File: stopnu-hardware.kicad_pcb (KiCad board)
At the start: 4 copper layers, 94 x 131 mm, 108 parts, among them CN1 SM04B-SRSS-TB (LF)(SN), CN2 OQ0232510000G, CN3 OQ0232510000G, CN4 OQ0232510000G, CN5 OQ0232510000G, CN6 OQ0232510000G, CN7 OQ0232510000G, CN8 OQ0232510000G, J1 Conn_02x15_Odd_Even, J2 Conn_01x02_Pin, U1 WIFI_KIT_32__V3_, U19 SY6280AAC, U2 74HCT1G125GW-Q100H, U3 LD1117V33, U4 74HCT1G125GW-Q100H, U5 LTV-817S, U6 LTV-817S, U7 LTV-817S, U8 MPU-6050_C24112

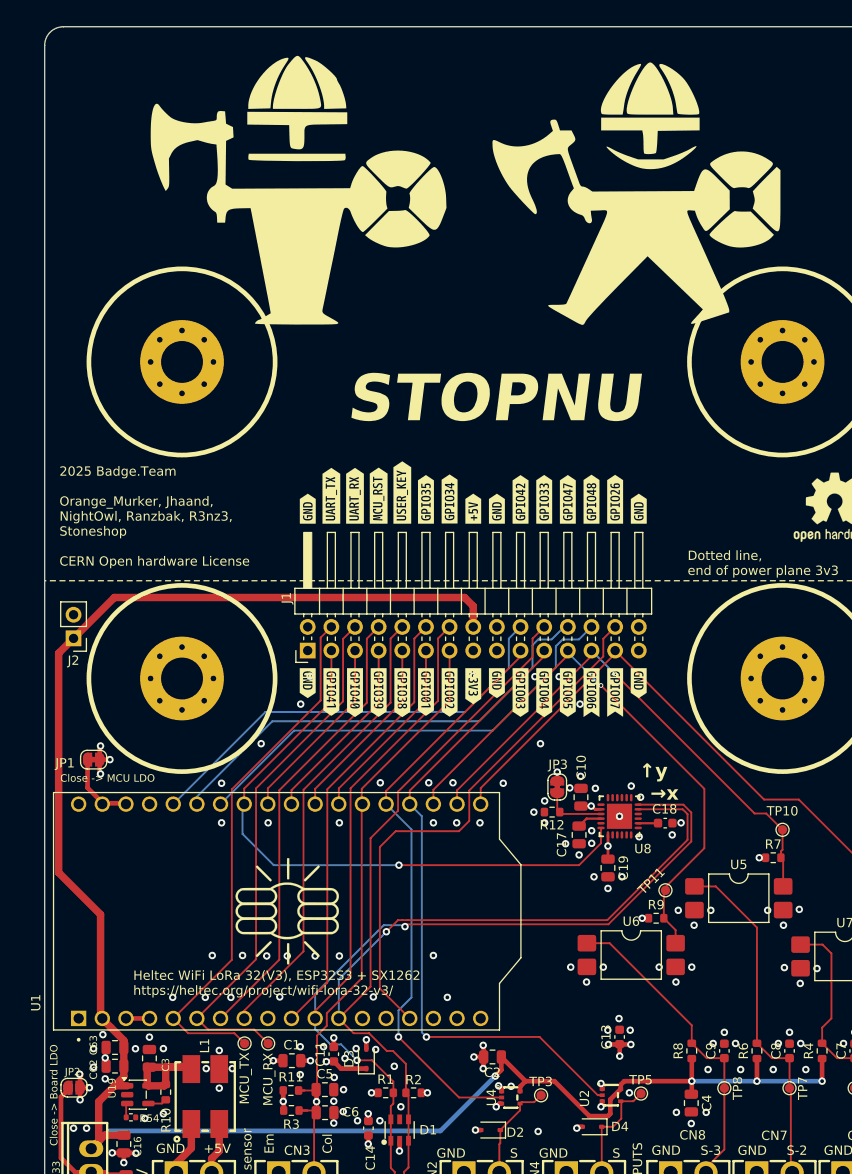
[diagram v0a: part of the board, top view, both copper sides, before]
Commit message: Update viking footprint art.
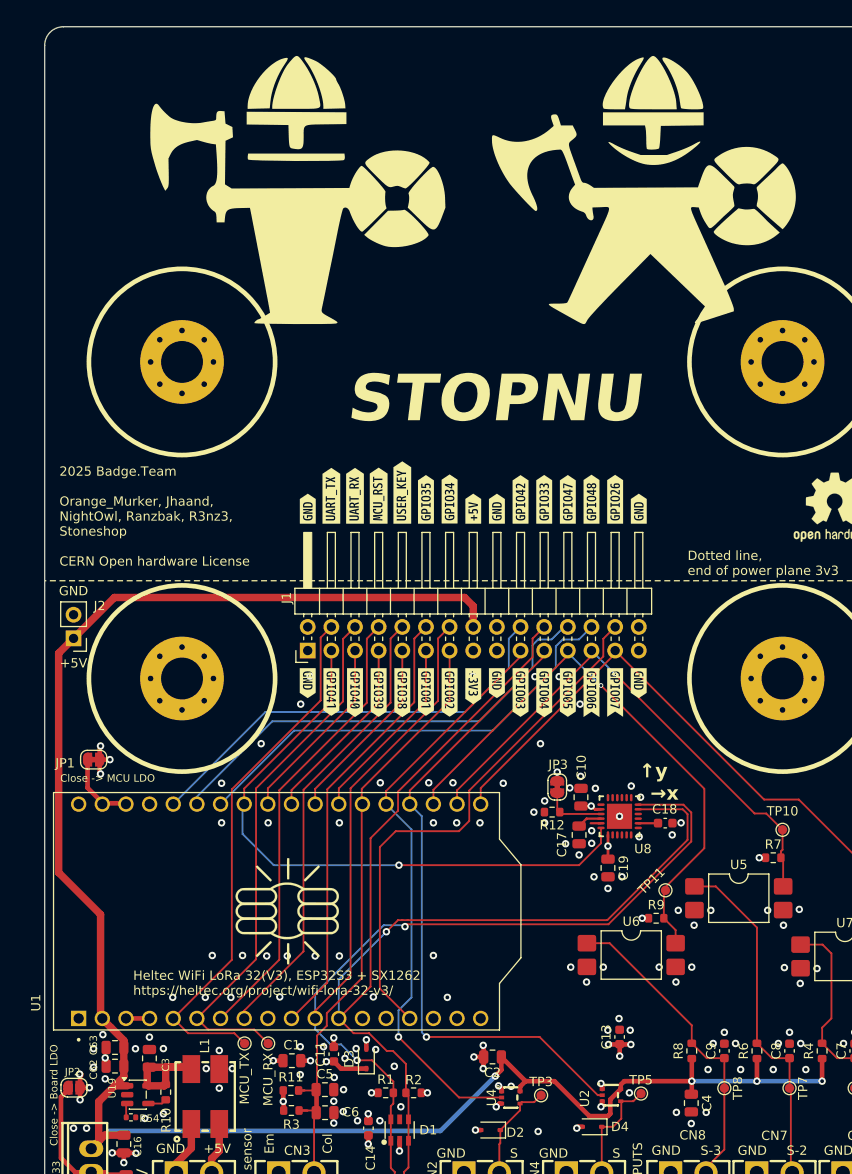
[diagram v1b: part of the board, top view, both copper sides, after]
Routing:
- net /GPIO02: track 67.8 -> 66.6 mm, vias 1 -> 0
- net GND: track 24.3 -> 25.4 mm
- net Net-(JP3-B): track 6.67 -> 6.00 mm

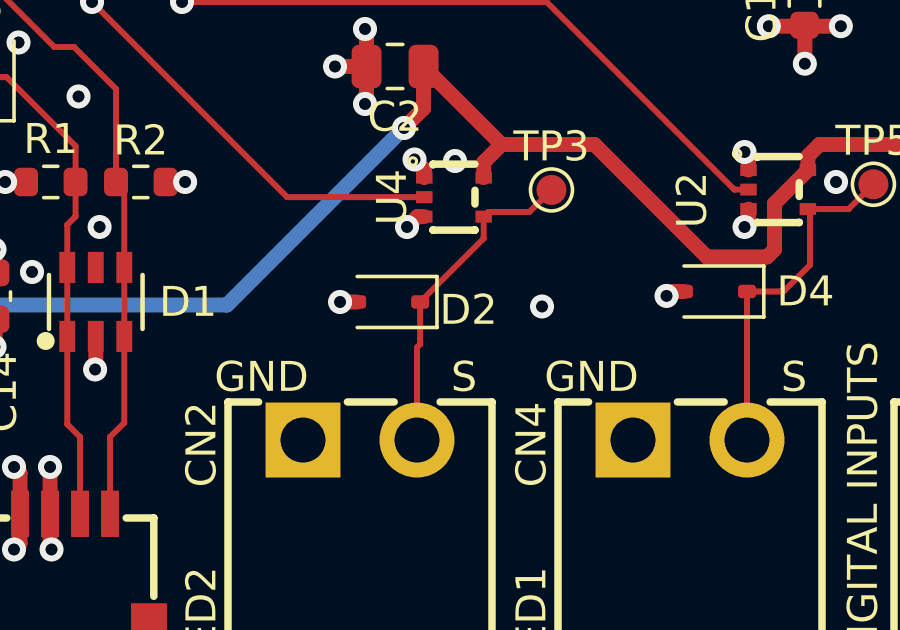
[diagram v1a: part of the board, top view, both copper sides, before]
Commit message: Straightened a track between D2 and CN2
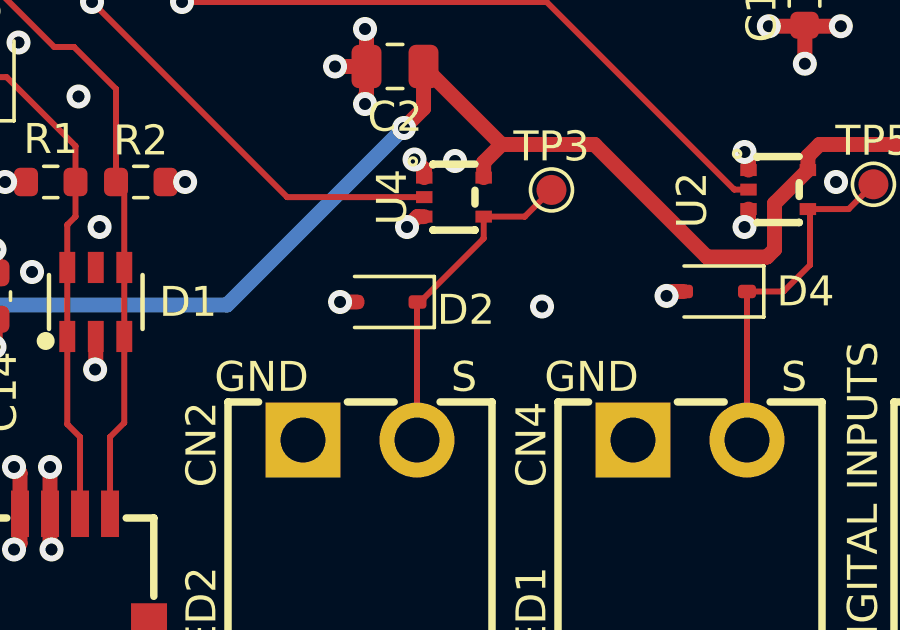
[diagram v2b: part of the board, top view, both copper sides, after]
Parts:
- moved D2 0.09 mm to (0.80, 65.5)

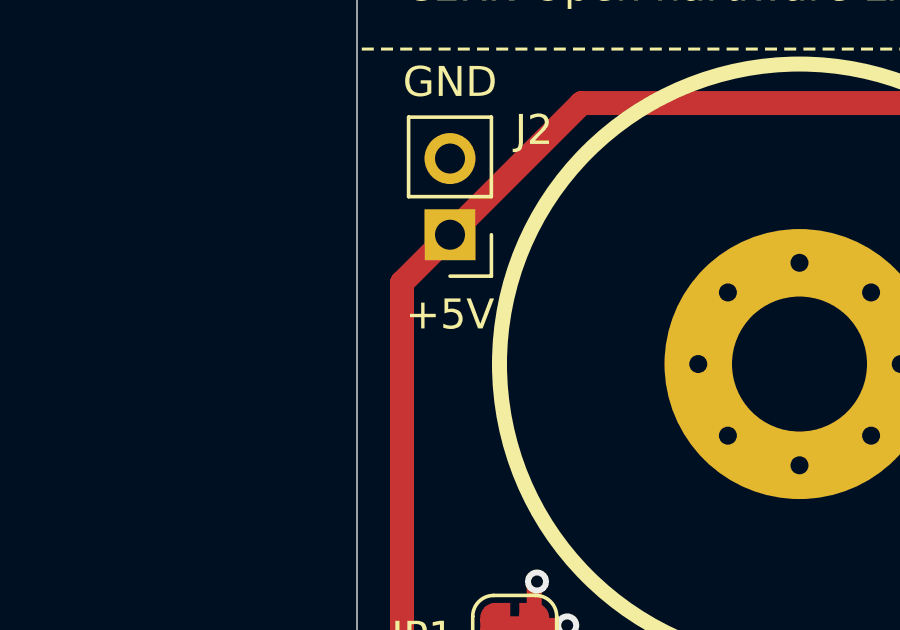
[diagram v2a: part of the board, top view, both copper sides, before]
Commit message: Fixed fabrication files, so PCBA will work with the correct rotation of the components.
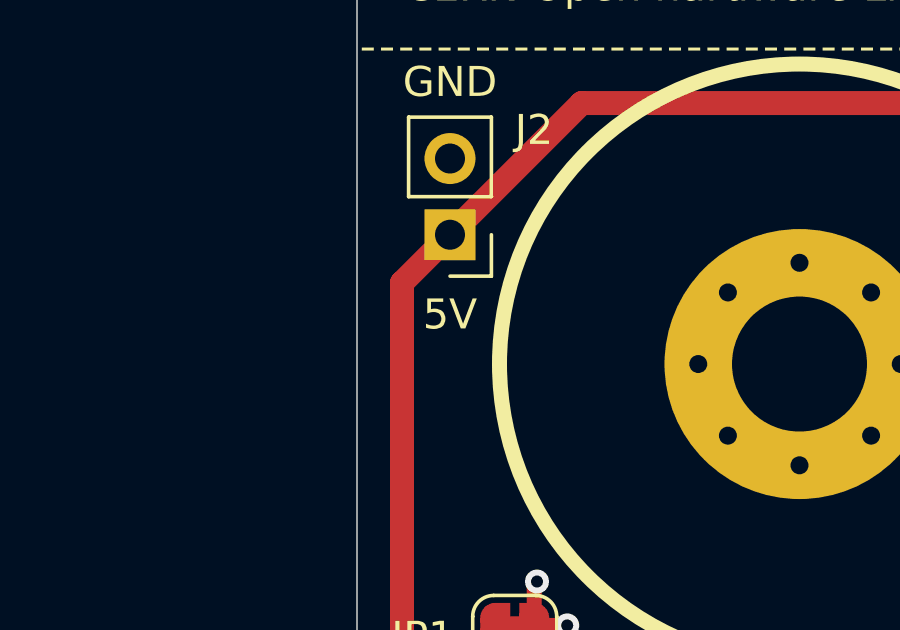
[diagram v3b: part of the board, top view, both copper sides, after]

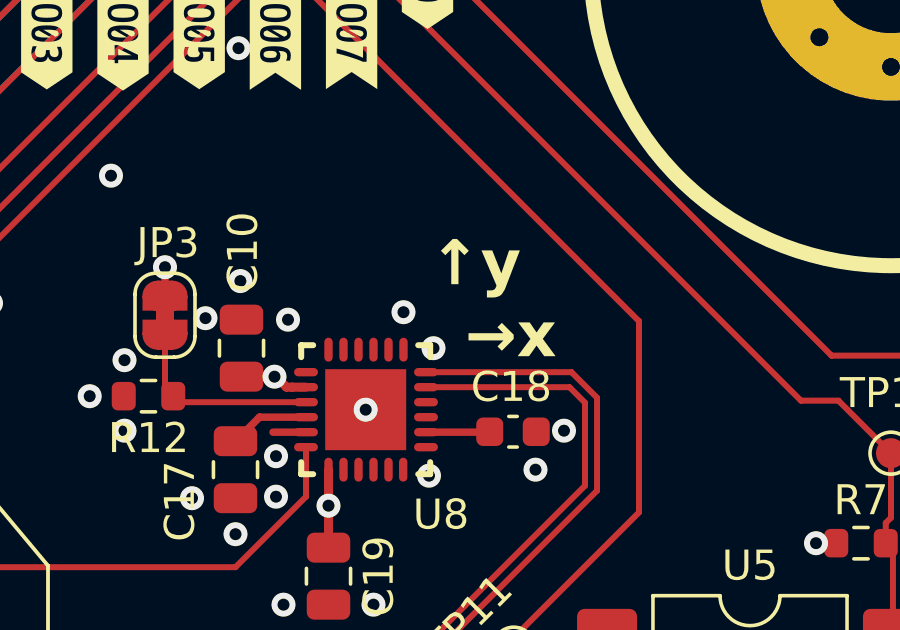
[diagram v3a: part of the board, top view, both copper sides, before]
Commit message: Add orientation mark for accelerometer.
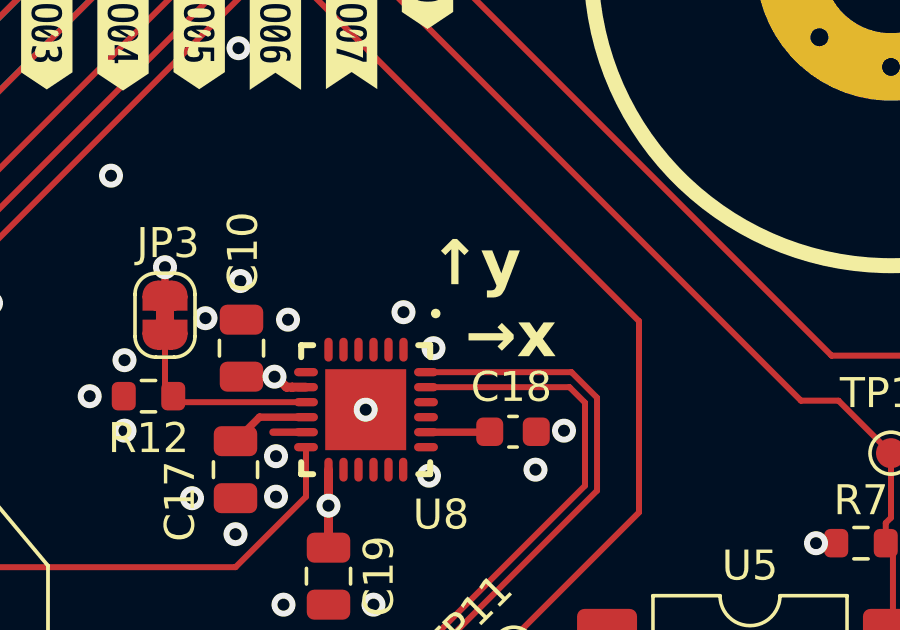
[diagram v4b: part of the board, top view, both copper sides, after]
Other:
- board text added: "•"
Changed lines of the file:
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@@
+		)
+	)
+	(gr_text "•"
+		(at 16.75 29.1 0)
+		(layer "F.SilkS")
+		(effects
+			(font
+				(size 0.8 0.8)
+				(thickness 0.1)
+			)
+			(justify left bottom)
 		)
 	)

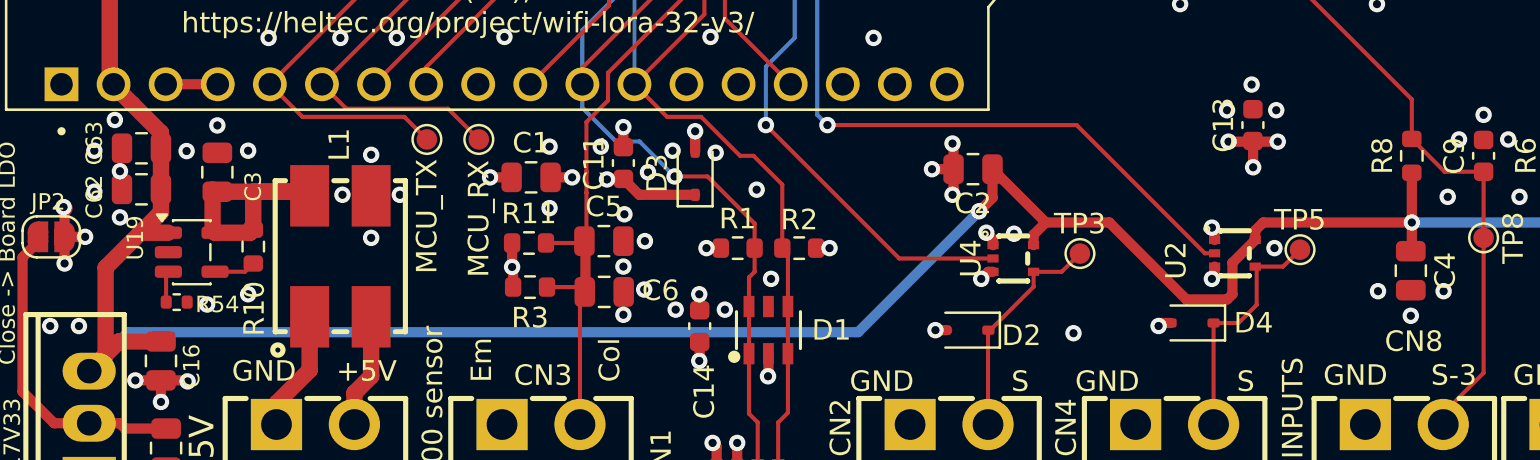
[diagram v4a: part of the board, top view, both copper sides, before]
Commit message: Fixed issue with too little of a component for second prod run.
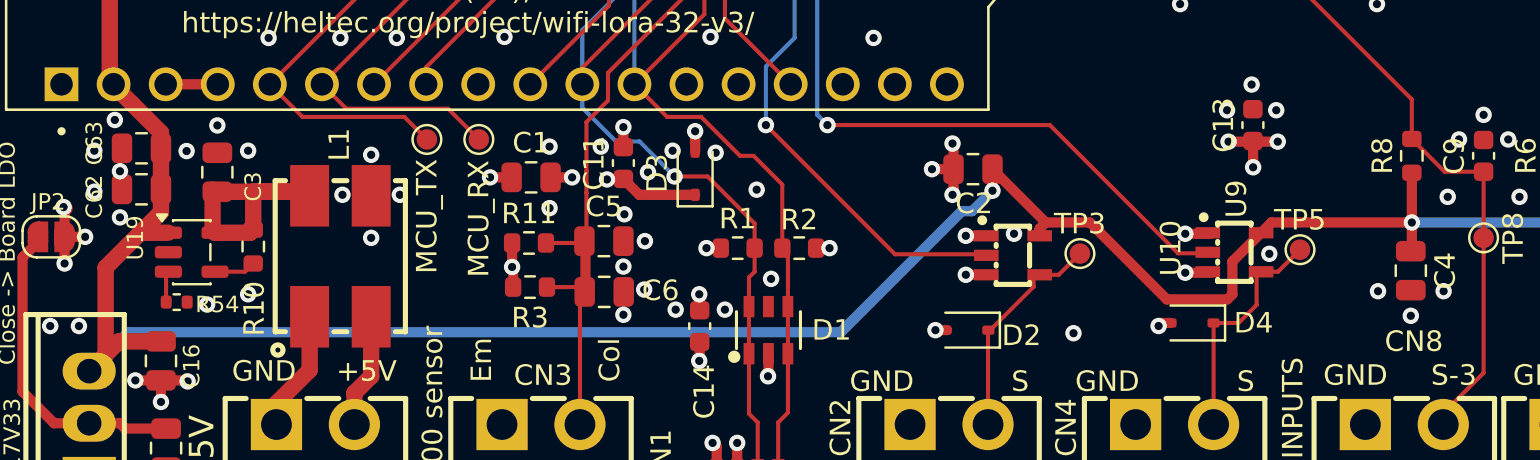
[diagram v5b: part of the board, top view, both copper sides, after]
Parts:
- removed U2, U4: 74HCT1G125GW-Q100H, lcsc:TSSOP-5_L2.1-W1.3-P0.65-LS2.2-BL
- added U10: 74HCT1G125GV,125, lcsc:SOT-753_L3.1-W1.7-P0.95-LS3.0-BL, F.Cu at (3.05, 61.9)
- added U9: 74HCT1G125GV,125, lcsc:SOT-753_L3.1-W1.7-P0.95-LS3.0-BL, F.Cu at (13.8, 61.7)
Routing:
- net GND: track 25.4 -> 27.3 mm
- net +5V: track 211.3 -> 210.6 mm
